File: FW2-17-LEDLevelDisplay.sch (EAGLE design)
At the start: 60 parts, among them Q1 BC557, Q10 BC547, Q11 BC547, Q2 BC547, Q3 BC547, Q4 BC547, Q5 BC547, Q6 BC547, Q7 BC547, Q8 BC547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

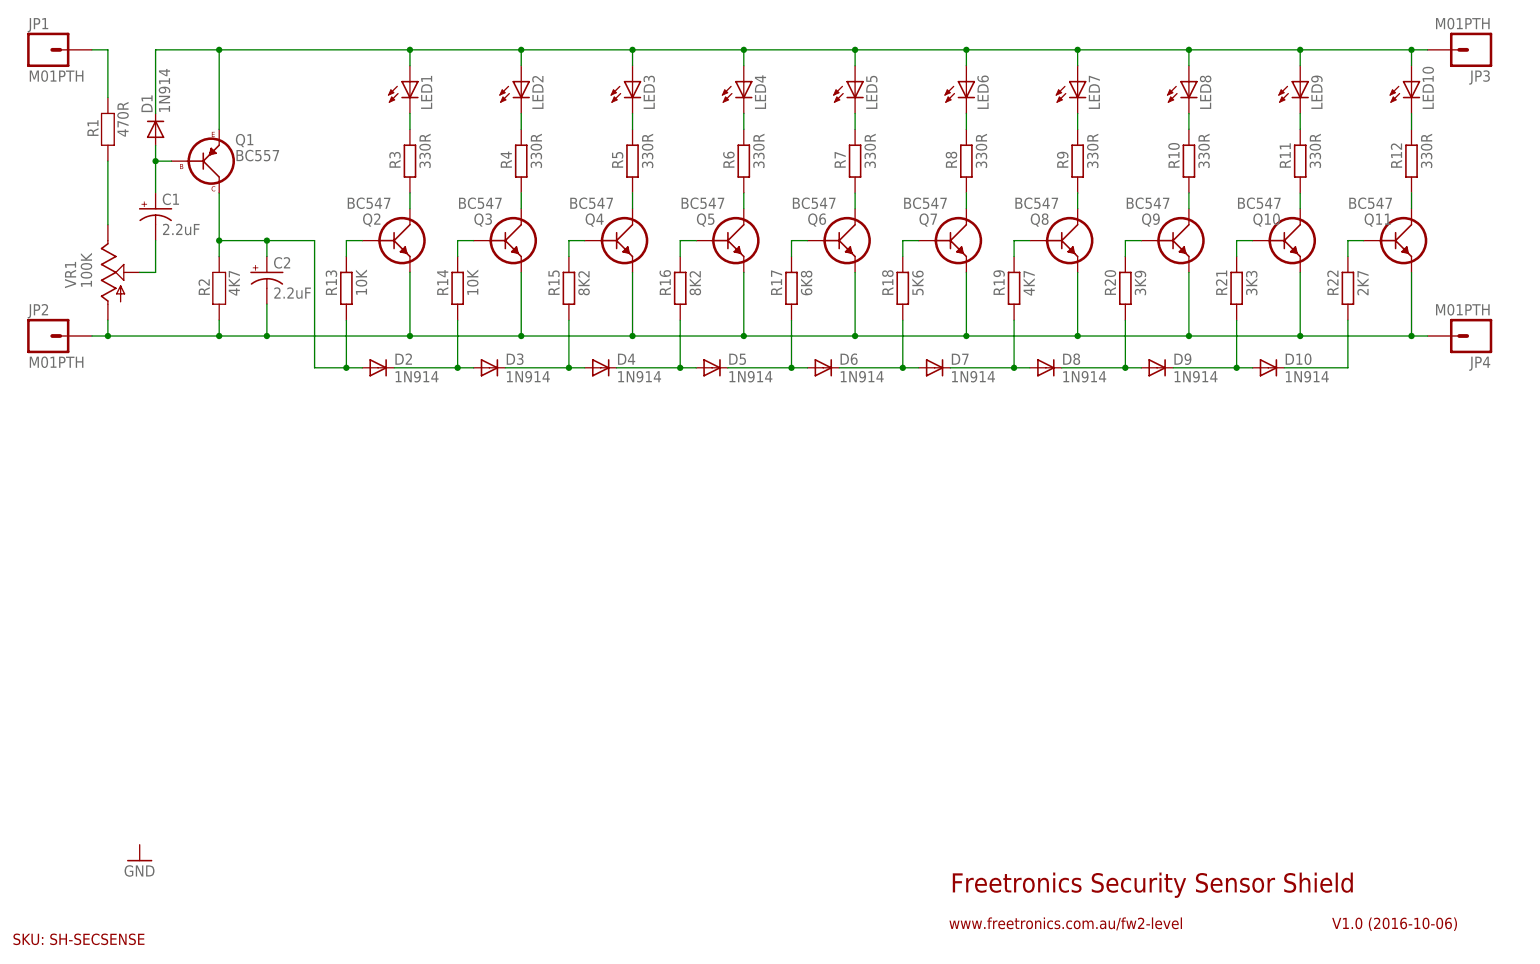
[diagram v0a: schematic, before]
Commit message: Reduced size of diode footprints; fixed part values
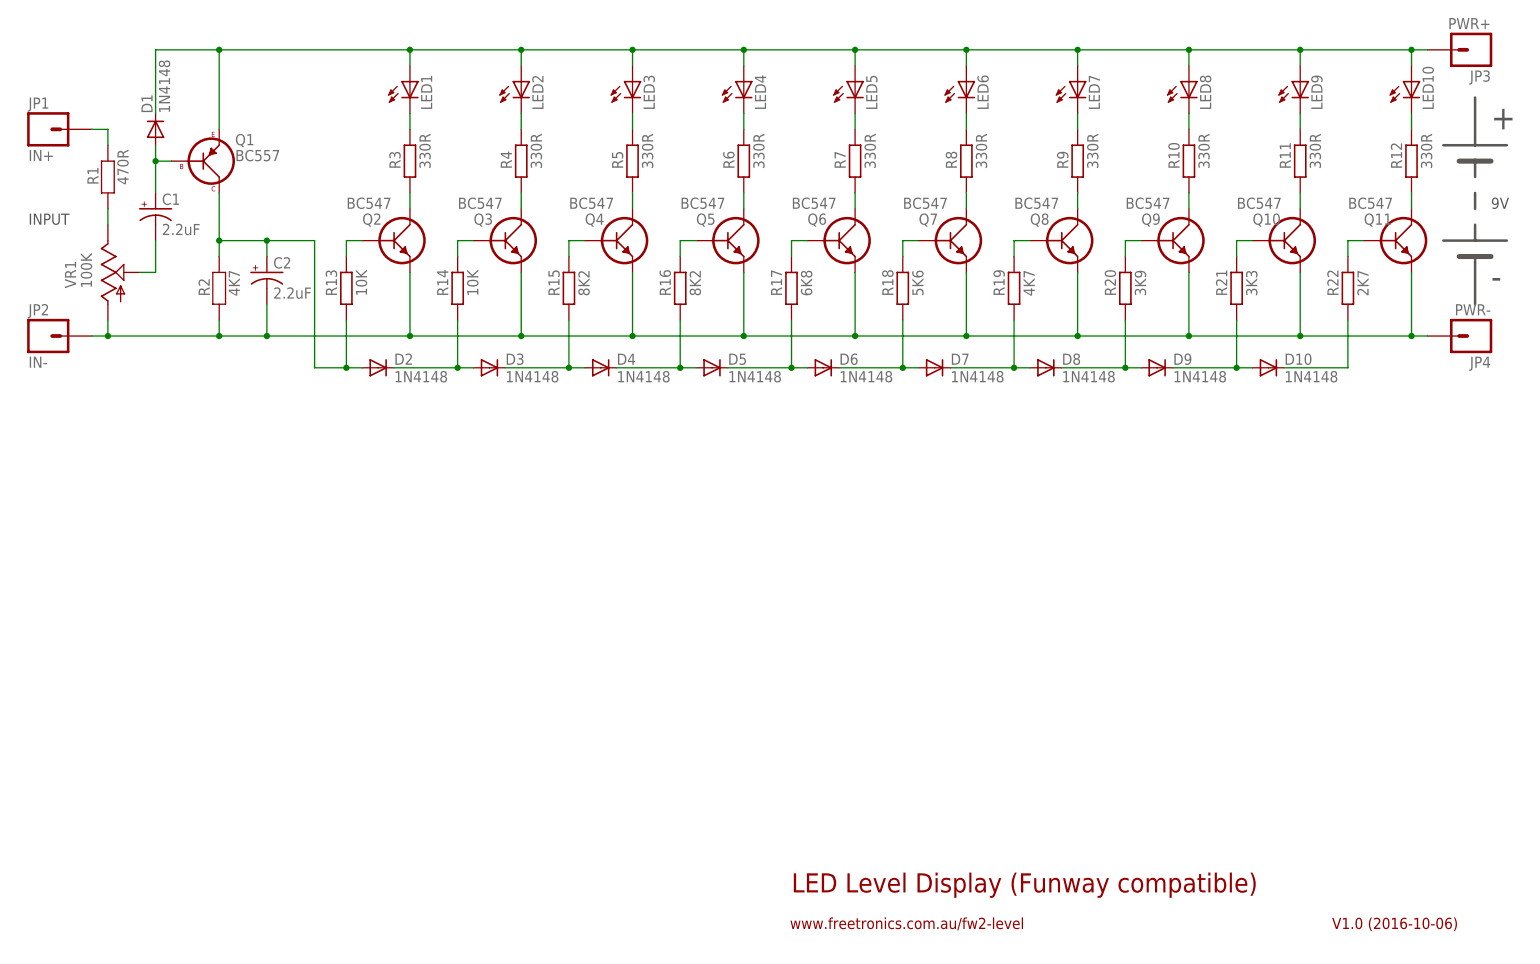
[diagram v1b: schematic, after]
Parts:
- D1, D10, D2, D3, D4, D5, D6, D7, D8, D9: value 1N914 -> 1N4148; device freetronics-master-v1.1:DIODE1N4148 -> freetronics-master-v1.1:DIODE1N914
- JP1: value M01PTH -> IN+
- JP2: value M01PTH -> IN-
- JP3: value M01PTH -> PWR+
- JP4: value M01PTH -> PWR-
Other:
- note added: "+"
- note added: "-"
- note added: "9V"
- note added: "INPUT"
- note added: "LED Level Display (Funway compatible)"
- note removed: "Freetronics Security Sensor Shield"
- note removed: "SKU: SH-SECSENSE"
- moved on the sheet: JP1, R1
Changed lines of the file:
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@@
 <part name="R4" library="resistor" deviceset="R-EU_" device="0309/V" value="330R"/>
 <part name="LED2" library="freetronics-master-v1.1" deviceset="LED" device="5MM"/>
-<part name="D2" library="freetronics-master-v1.1" deviceset="DIODE" device="1N4148" value="1N914"/>
-<part name="D3" library="freetronics-master-v1.1" deviceset="DIODE" device="1N4148" value="1N914"/>
-<part name="D4" library="freetronics-master-v1.1" deviceset="DIODE" device="1N4148" value="1N914"/>
-<part name="D5" library="freetronics-master-v1.1" deviceset="DIODE" device="1N4148" value="1N914"/>
-<part name="D6" library="freetronics-master-v1.1" deviceset="DIODE" device="1N4148" value="1N914"/>
+<part name="D2" library="freetronics-master-v1.1" deviceset="DIODE" device="1N914" value="1N4148"/>
+<part name="D3" library="freetronics-master-v1.1" deviceset="DIODE" device="1N914" value="1N4148"/>
+<part name="D4" library="freetronics-master-v1.1" deviceset="DIODE" device="1N914" value="1N4148"/>
+<part name="D5" library="freetronics-master-v1.1" deviceset="DIODE" device="1N914" value="1N4148"/>
+<part name="D6" library="freetronics-master-v1.1" deviceset="DIODE" device="1N914" value="1N4148"/>
 <part name="Q4" library="freetronics-master-v1.1" deviceset="BC547" device=""/>
 <part name="Q5" library="freetronics-master-v1.1" deviceset="BC547" device=""/>
@@
 <part name="LED8" library="freetronics-master-v1.1" deviceset="LED" device="5MM"/>
 <part name="LED9" library="freetronics-master-v1.1" deviceset="LED" device="5MM"/>
-<part name="D7" library="freetronics-master-v1.1" deviceset="DIODE" device="1N4148" value="1N914"/>
-<part name="D8" library="freetronics-master-v1.1" deviceset="DIODE" device="1N4148" value="1N914"/>
-<part name="D9" library="freetronics-master-v1.1" deviceset="DIODE" device="1N4148" value="1N914"/>
-<part name="JP1" library="freetronics-master-v1.1" deviceset="M01" device="PTH"/>
-<part name="JP2" library="freetronics-master-v1.1" deviceset="M01" device="PTH"/>
-<part name="JP3" library="freetronics-master-v1.1" deviceset="M01" device="PTH"/>
-<part name="JP4" library="freetronics-master-v1.1" deviceset="M01" device="PTH"/>
-<part name="GND1" library="freetronics-original" deviceset="GND" device=""/>
+<part name="D7" library="freetronics-master-v1.1" deviceset="DIODE" device="1N914" value="1N4148"/>
+<part name="D8" library="freetronics-master-v1.1" deviceset="DIODE" device="1N914" value="1N4148"/>
+<part name="D9" library="freetronics-master-v1.1" deviceset="DIODE" device="1N914" value="1N4148"/>
+<part name="JP1" library="freetronics-master-v1.1" deviceset="M01" device="PTH" value="IN+"/>
+<part name="JP2" library="freetronics-master-v1.1" deviceset="M01" device="PTH" value="IN-"/>
+<part name="JP3" library="freetronics-master-v1.1" deviceset="M01" device="PTH" value="PWR+"/>
+<part name="JP4" library="freetronics-master-v1.1" deviceset="M01" device="PTH" value="PWR-"/>
 <part name="C2" library="SparkFun" deviceset="CAP_POL" device="PTH1" value="2.2uF"/>
 <part name="C1" library="SparkFun" deviceset="CAP_POL" device="PTH1" value="2.2uF"/>
@@
 <part name="Q11" library="freetronics-master-v1.1" deviceset="BC547" device=""/>
 <part name="R22" library="resistor" deviceset="R-EU_" device="0309/V" value="2K7"/>
-<part name="D10" library="freetronics-master-v1.1" deviceset="DIODE" device="1N4148" value="1N914"/>
-<part name="D1" library="freetronics-master-v1.1" deviceset="DIODE" device="1N4148" value="1N914"/>
+<part name="D10" library="freetronics-master-v1.1" deviceset="DIODE" device="1N914" value="1N4148"/>
+<part name="D1" library="freetronics-master-v1.1" deviceset="DIODE" device="1N914" value="1N4148"/>
 <part name="R1" library="freetronics" deviceset="FREETRONICS_RESISTOR" device="PTH2" value="470R"/>
 <part name="Q1" library="freetronics-master-v1.1" deviceset="BC557" device=""/>
@@
 <sheet>
 <plain>
-<text x="154.94" y="12.7" size="3.048" layer="94">Freetronics Security Sensor Shield</text>
+<text x="129.54" y="12.7" size="3.048" layer="94">LED Level Display (Funway compatible)</text>
 <text x="215.9" y="6.858" size="1.778" layer="94">V1.0 (2016-10-06)</text>
-<text x="5.08" y="4.318" size="1.778" layer="94">SKU: SH-SECSENSE</text>
-<text x="154.686" y="6.858" size="1.778" layer="94">www.freetronics.com.au/fw2-level</text>
+<text x="129.286" y="6.858" size="1.778" layer="94">www.freetronics.com.au/fw2-level</text>
 <frame x1="0" y1="0" x2="248.92" y2="185.42" columns="8" rows="5" layer="94"/>
-<frame x1="152.4" y1="5.08" x2="243.84" y2="17.78" columns="0" rows="0" layer="94" border-left="no" border-top="no" border-right="no" border-bottom="no"/>
-<frame x1="152.4" y1="5.08" x2="213.36" y2="10.16" columns="8" rows="5" layer="94"/>
+<frame x1="127" y1="5.08" x2="243.84" y2="17.78" columns="0" rows="0" layer="94" border-left="no" border-top="no" border-right="no" border-bottom="no"/>
+<frame x1="127" y1="5.08" x2="187.96" y2="10.16" columns="8" rows="5" layer="94"/>
 <frame x1="213.36" y1="5.08" x2="243.84" y2="10.16" columns="8" rows="5" layer="94"/>
+<wire x1="233.68" y1="132.08" x2="238.76" y2="132.08" width="0.4064" layer="97"/>
+<wire x1="238.76" y1="132.08" x2="243.84" y2="132.08" width="0.4064" layer="97"/>
+<wire x1="236.22" y1="129.54" x2="238.76" y2="129.54" width="0.8128" layer="97"/>
+<wire x1="238.76" y1="129.54" x2="241.3" y2="129.54" width="0.8128" layer="97"/>
+<wire x1="233.68" y1="116.84" x2="243.84" y2="116.84" width="0.4064" layer="97"/>
+<wire x1="236.22" y1="114.3" x2="238.76" y2="114.3" width="0.8128" layer="97"/>
+<wire x1="238.76" y1="114.3" x2="241.3" y2="114.3" width="0.8128" layer="97"/>
+<wire x1="238.76" y1="124.46" x2="238.76" y2="121.92" width="0.4064" layer="97"/>
+<wire x1="238.76" y1="119.38" x2="238.76" y2="116.84" width="0.4064" layer="97"/>
+<wire x1="238.76" y1="132.08" x2="238.76" y2="139.7" width="0.4064" layer="97"/>
+<wire x1="238.76" y1="114.3" x2="238.76" y2="106.68" width="0.4064" layer="97"/>
+<wire x1="238.76" y1="127" x2="238.76" y2="129.54" width="0.4064" layer="97"/>
+<text x="241.3" y="121.92" size="1.778" layer="97" ratio="15">9V</text>
+<text x="241.3" y="134.62" size="3.81" layer="97" ratio="15">+</text>
+<text x="241.3" y="109.22" size="3.81" layer="97" ratio="15">-</text>
+<text x="7.62" y="119.38" size="1.778" layer="97" ratio="15">INPUT</text>
 </plain>
 <instances>
@@
 <instance part="D8" gate="G$1" x="170.18" y="96.52"/>
 <instance part="D9" gate="G$1" x="187.96" y="96.52"/>
-<instance part="JP1" gate="G$1" x="10.16" y="147.32"/>
+<instance part="JP1" gate="G$1" x="10.16" y="134.62"/>
 <instance part="JP2" gate="G$1" x="10.16" y="101.6"/>
 <instance part="JP3" gate="G$1" x="238.76" y="147.32" rot="R180"/>
 <instance part="JP4" gate="G$1" x="238.76" y="101.6" rot="R180"/>
-<instance part="GND1" gate="1" x="25.4" y="17.78"/>
 <instance part="C2" gate="G$1" x="45.72" y="111.76"/>
 <instance part="C1" gate="G$1" x="27.94" y="121.92"/>
@@
 <instance part="D10" gate="G$1" x="205.74" y="96.52"/>
 <instance part="D1" gate="G$1" x="27.94" y="134.62" rot="R90"/>
-<instance part="R1" gate="G$1" x="20.32" y="134.62" smashed="yes" rot="R90">
-<attribute name="NAME" x="18.8214" y="133.35" size="1.778" layer="95" rot="R90"/>
-<attribute name="VALUE" x="23.622" y="133.35" size="1.778" layer="96" rot="R90"/>
+<instance part="R1" gate="G$1" x="20.32" y="127" smashed="yes" rot="R90">
+<attribute name="NAME" x="18.8214" y="125.73" size="1.778" layer="95" rot="R90"/>
+<attribute name="VALUE" x="23.622" y="125.73" size="1.778" layer="96" rot="R90"/>
 </instance>
 <instance part="Q1" gate="G$1" x="35.56" y="129.54"/>
@@
 <pinref part="VR1" gate="G$1" pin="E"/>
 <pinref part="R1" gate="G$1" pin="1"/>
-<wire x1="20.32" y1="119.38" x2="20.32" y2="129.54" width="0.1524" layer="91"/>
+<wire x1="20.32" y1="119.38" x2="20.32" y2="121.92" width="0.1524" layer="91"/>
 </segment>
 </net>
@@
 <segment>
 <pinref part="R1" gate="G$1" pin="2"/>
-<wire x1="20.32" y1="139.7" x2="20.32" y2="147.32" width="0.1524" layer="91"/>
+<wire x1="20.32" y1="132.08" x2="20.32" y2="134.62" width="0.1524" layer="91"/>
 <pinref part="JP1" gate="G$1" pin="1"/>
-<wire x1="20.32" y1="147.32" x2="17.78" y2="147.32" width="0.1524" layer="91"/>
-</segment>
-</net>
+<wire x1="20.32" y1="134.62" x2="17.78" y2="134.62" width="0.1524" layer="91"/>
+</segment>
+</net>

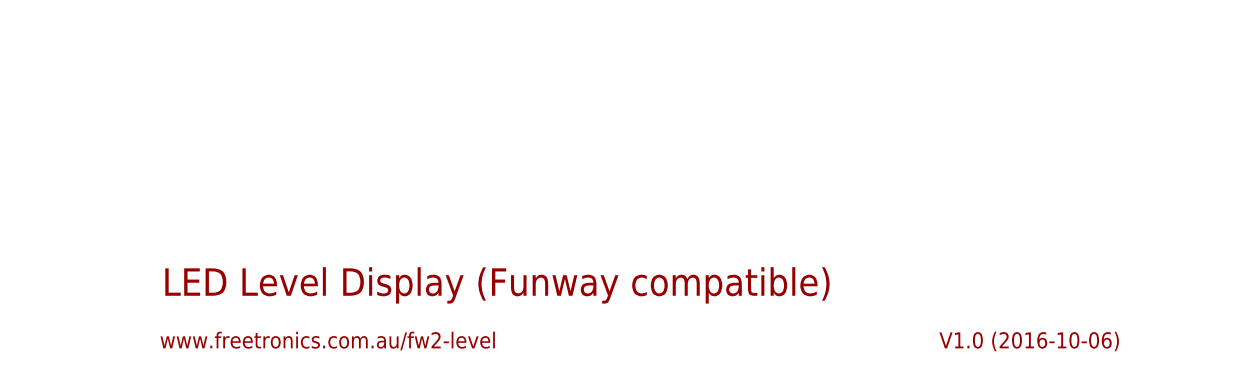
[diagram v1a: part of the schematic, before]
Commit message: Updated silkscreen and labels
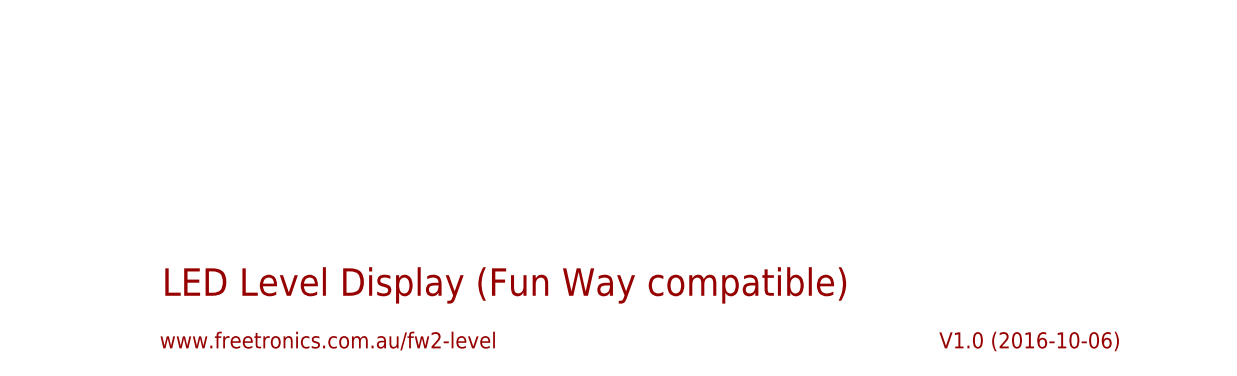
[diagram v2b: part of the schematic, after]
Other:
- note added: "LED Level Display (Fun Way compatible)"
- note removed: "LED Level Display (Funway compatible)"
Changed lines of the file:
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@@
 <sheet>
 <plain>
-<text x="129.54" y="12.7" size="3.048" layer="94">LED Level Display (Funway compatible)</text>
+<text x="129.54" y="12.7" size="3.048" layer="94">LED Level Display (Fun Way compatible)</text>
 <text x="215.9" y="6.858" size="1.778" layer="94">V1.0 (2016-10-06)</text>
 <text x="129.286" y="6.858" size="1.778" layer="94">www.freetronics.com.au/fw2-level</text>
